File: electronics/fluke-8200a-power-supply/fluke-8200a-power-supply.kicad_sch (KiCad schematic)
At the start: 66 parts, among them J1 Conn_01x08, J2 Conn_01x03, Q1 NPN, Q10 NPN, Q11 2N3055, Q12 NPN, Q13 NPN, Q2 NPN, Q3 NPN, Q4 NPN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

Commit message: only need correct transistors now
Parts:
- removed J2: Conn_01x03, symbol Connector_Generic:Conn_01x03
- removed Q6: NPN, symbol Simulation_SPICE:NPN
- removed R15: R_US, symbol Device:R_US
- added C13: 0.01uF, symbol Device:C
- added J2: Conn_02x03_Counter_Clockwise, symbol Connector_Generic:Conn_02x03_Counter_Clockwise
- added Q6: PNP, symbol Simulation_SPICE:PNP
- C1: value C -> 8uF
- C10, C11, C6, C7, C8, C9: value C -> 1000uF
- C12: value C -> 0.047uF
- C2: value C -> 400
- C3: value C -> 125uF
- C4: value C -> 400uF
- C5: value C -> 125
- R1: value R_US -> 510
- R10: value R_US -> 5.1K
- R11: value R_US -> 78.7K
- R12: value R_Potentiometer_Trim_US -> 10K
- R13: renamed from R21; value R_US -> 59.0K
- R14: value R_US -> 10.0K
- R16, R6: value R_US -> 33
- R18: renamed from R12; value R_US -> 9.09K
- R19: renamed from R13; value R_US -> 33K
- R2: value R_US -> 33K
- R21: renamed from R20; value R_US -> 4.7K
- R22: renamed from R19; value R_US -> 5.6K
- R23: renamed from R18; value R_US -> 10K
- R24: renamed from R17; value R_US -> 33.2K
- R3: value R_US -> 182K
- R4: value R_US -> 15.4K
- R5, R7: value R_US -> 1M
- R8: value R_US -> 470K
- R9: value R_US -> 4.7K
- renumbered D13 to D10, D9 to D13, D10 to D14, D12 to D15, D11 to D16, D14 to D9
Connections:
- net at D15.1 (K): now also D13.2 (A), J1.4 (Pin_4); no longer D16.1 (K)
- net GND: now reaches D15.2 (A)
- net GND: now also C1.1, C10.2, C11.2, C6.2, C7.2, C8.2, C9.2, D1.2 (A), D16.2 (A), D3.2 (A), Q13.3 (E), J2.2 (Pin_2)
- net +5V: now reaches TP5.1
- net +5V: now also Q11.2 (E), R22.2, R23.2, J2.6 (Pin_6)
- net GNDS: now reaches TP3.1
- net GNDS: now also C12.1, C2.1, C3.1, C4.2, C5.1, D9.2 (A), J1.8 (Pin_8), Q7.1 (C), R13.2, R4.1, J2.5 (Pin_5), Q6.3 (E)
- net at C7.1: now also C10.1, C11.1, C6.1, C8.1, C9.1, D13.1 (K), D14.1 (K), Q11.3 (C), Q12.1 (C)
- net +200V: now reaches R5.1
- net +200V: now also Q1.3 (E), R3.2, TP1.1, J2.3 (Pin_3)
- net at R5.2: now also C12.2, R7.1
- net at R23.1: now also Q13.2 (B), R24.2
- net at Q5.1 (C): now also Q4.2 (B), R7.2
- net at Q5.2 (B): now also R12.2
- net at Q5.3 (E): now also D9.1 (K), R10.2
- net at R8.1: now also D10.2 (A), Q7.3 (E), Q6.2 (B)
- net at R8.2: now also Q10.3 (E), R16.2
- net at R1.1: now also C1.2, D2.1 (K), D4.1 (K), R2.1
- net at R1.2: now also Q1.1 (C); no longer R3.2
- net at R12.1: now also R13.1
- net at R12.3: now also R11.2
- net at D6.2 (A): now also D5.1 (K), J1.7 (Pin_7); no longer D5.2 (A)
- net at R22.1: now also Q11.1 (B), Q12.3 (E)
- net at D1.1 (K): now also D2.2 (A), J1.3 (Pin_3); no longer D2.1 (K)
- net at D7.2 (A): now also C4.1, D5.2 (A), R16.1; no longer D8.2 (A)
- net at Q1.2 (B): now also Q2.1 (C), R2.2
- net at R6.1: now also C2.2, D6.1 (K), D8.1 (K)
- net at R6.2: now also Q3.1 (C), Q4.1 (C)
- net at Q3.2 (B): now also Q4.3 (E)
- net +15V: now reaches Q3.3 (E)
- net +15V: now also C3.2, Q2.3 (E), R10.1, R11.1, R14.1, R21.2, TP2.1, J2.1 (Pin_1)
- net at D10.1 (K): now also R19.2
- net at R14.2: now also Q7.2 (B), R18.2, C13.1
- net at Q12.2 (B): now also Q13.1 (C), R21.1
- net -15V: now reaches R18.1
- net -15V: now also C5.2, Q10.1 (C), R19.1, R24.1, TP4.1, C13.2, J2.4 (Pin_4)
- net at J1.6 (Pin_6): now also D7.1 (K), D8.2 (A); no longer D14.1 (K)
- net at Q10.2 (B): now also R9.2
- net at R9.1: now also Q6.1 (C)
- net at Q2.2 (B): now also R3.1, R4.2
- new net: D3.1 (K), D4.2 (A), J1.2 (Pin_2)
- new net: D14.2 (A), D16.1 (K), J1.5 (Pin_5)
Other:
- moved on the sheet: C1, C12, C2, C3, C4, C5, C6, D1, D10, D13, D14, D15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

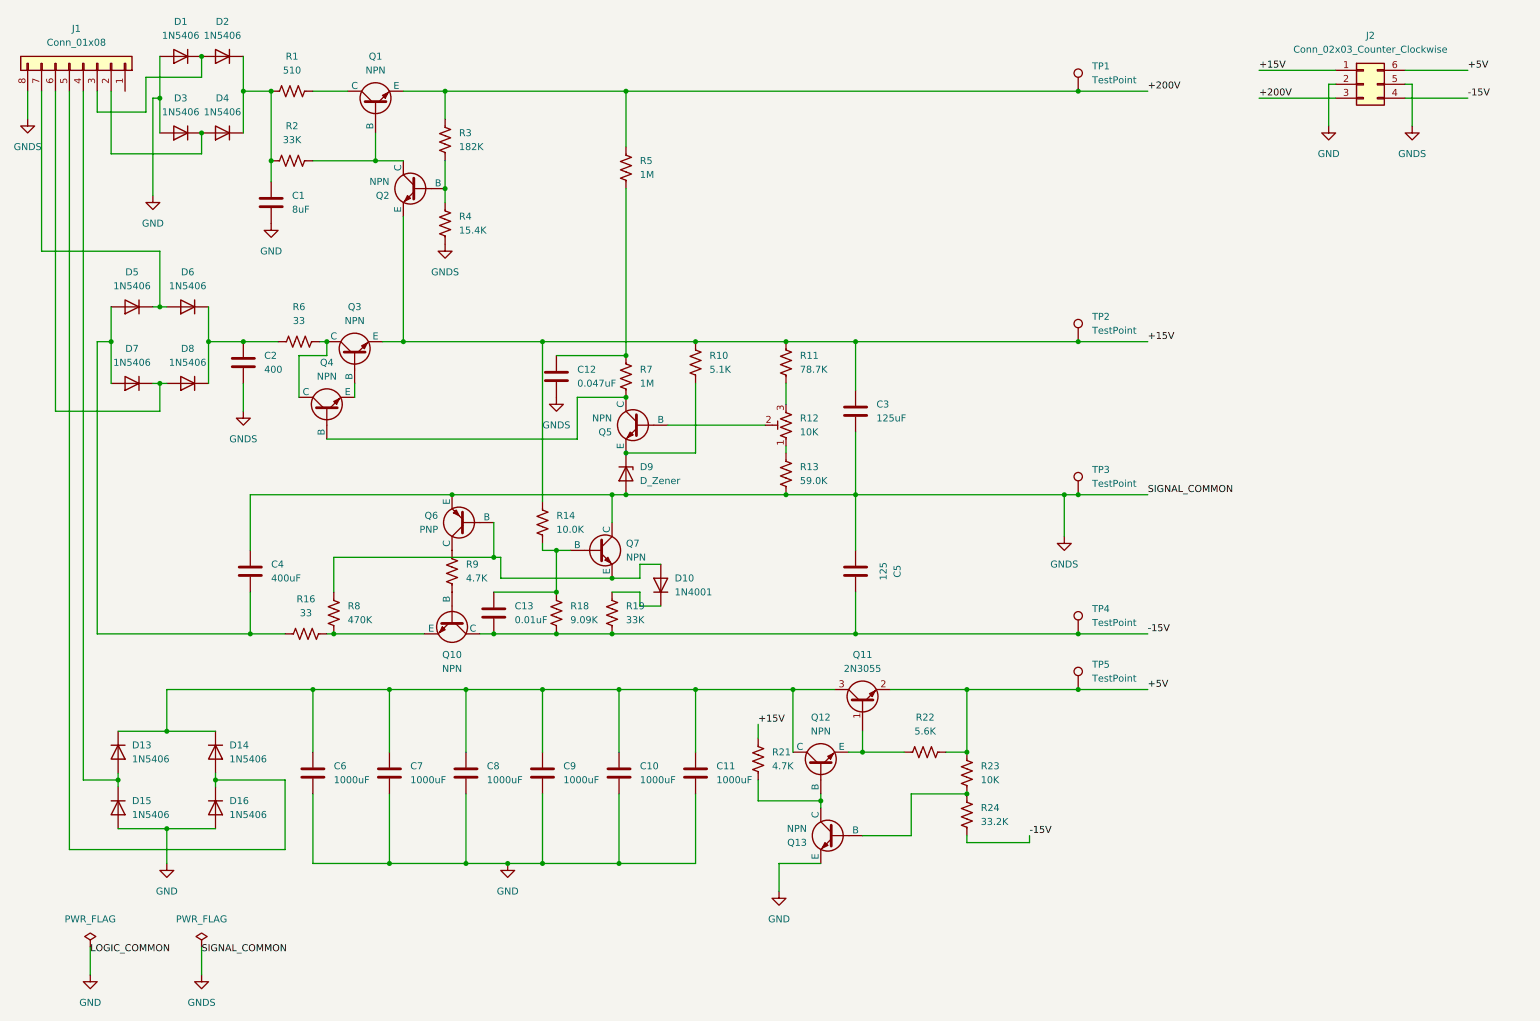
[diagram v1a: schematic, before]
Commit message: changed to pin headers
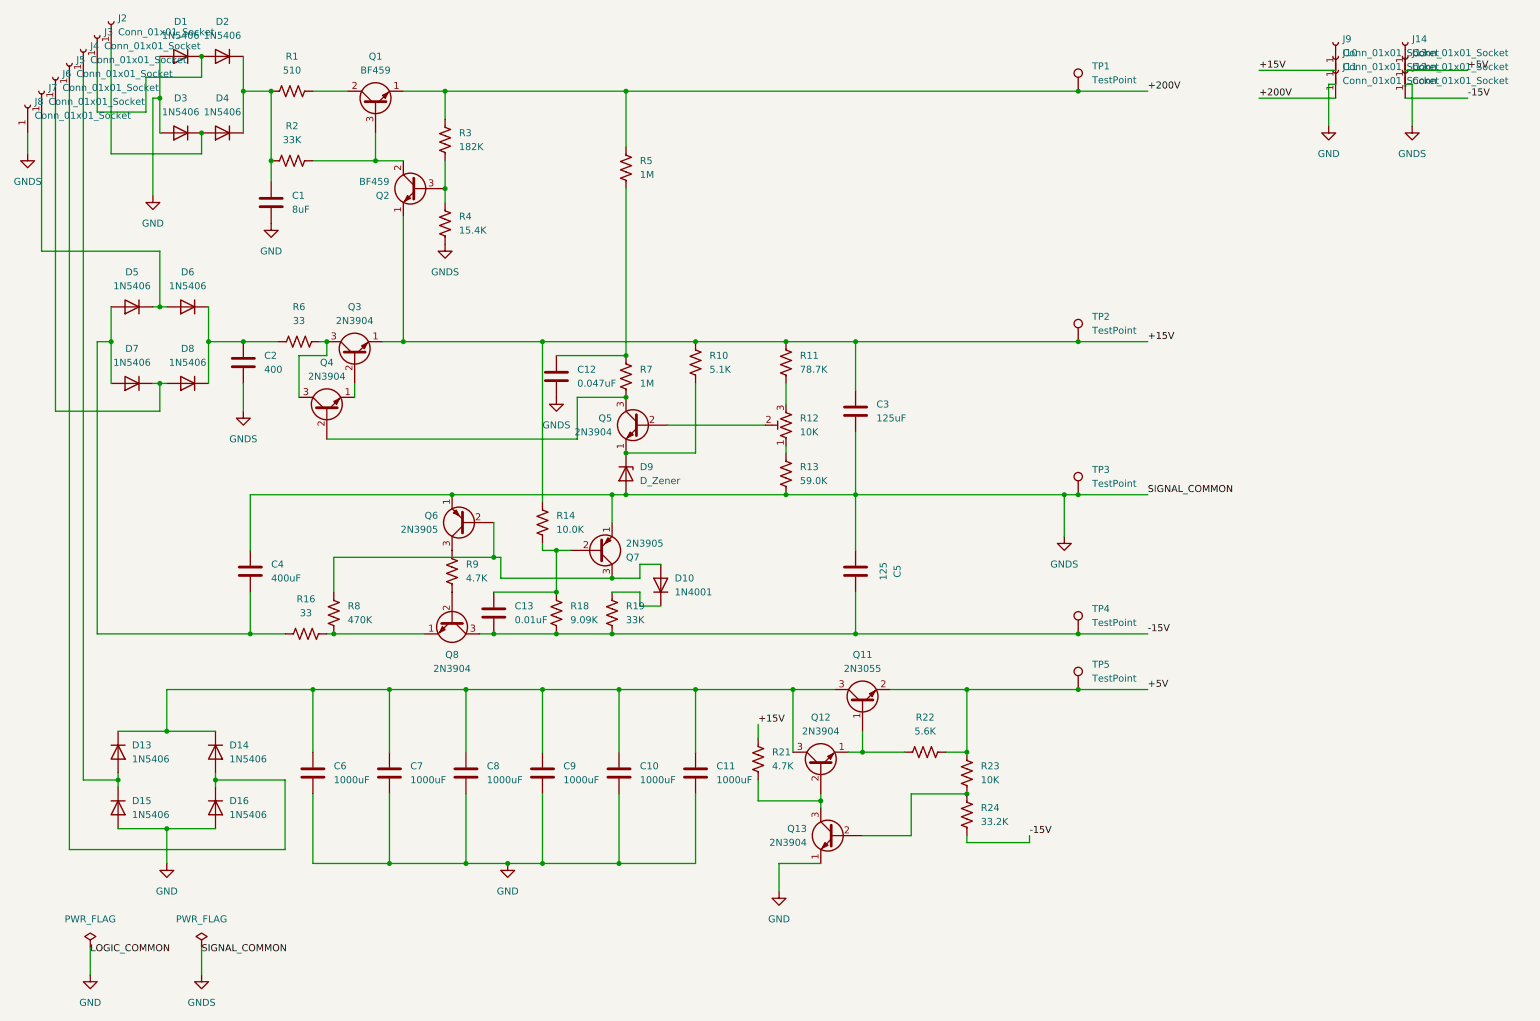
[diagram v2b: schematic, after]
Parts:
- removed J1: Conn_01x08, symbol Connector_Generic:Conn_01x08
- removed J2: Conn_02x03_Counter_Clockwise, symbol Connector_Generic:Conn_02x03_Counter_Clockwise
- removed Q1, Q10, Q12, Q13, Q2, Q3, Q4, Q5, Q7: NPN, symbol Simulation_SPICE:NPN
- removed Q6: PNP, symbol Simulation_SPICE:PNP
- added J10, J11, J12, J13, J14, J2, J3, J4, J5, J6, J7, J8, J9: Conn_01x01_Socket, Connector_PinSocket_2.54mm:PinSocket_1x01_P2.54mm_Vertical, symbol Connector:Conn_01x01_Socket
- added Q1, Q2: BF459, Package_TO_SOT_THT:TO-126-3_Vertical, symbol Transistor_BJT:BF459
- added Q12, Q13, Q3, Q4, Q5, Q8: 2N3904, Package_TO_SOT_THT:TO-92_Inline, symbol Transistor_BJT:2N3904
- added Q6, Q7: 2N3905, Package_TO_SOT_THT:TO-92_Inline, symbol Transistor_BJT:2N3905
- C1: footprint (none) -> Capacitor_THT:CP_Axial_L37.0mm_D13.0mm_P43.00mm_Horizontal
- C10, C11, C2, C4, C6, C7, C8, C9: footprint (none) -> Capacitor_THT:CP_Axial_L30.0mm_D10.0mm_P35.00mm_Horizontal
- C12: footprint (none) -> Capacitor_THT:C_Rect_L13.0mm_W4.0mm_P10.00mm_FKS3_FKP3_MKS4
- C13: footprint (none) -> Capacitor_THT:C_Disc_D8.0mm_W2.5mm_P5.00mm
- C3, C5: footprint (none) -> Capacitor_THT:CP_Axial_L18.0mm_D8.0mm_P25.00mm_Horizontal
- D10: footprint Diode_THT:D_DO-41_SOD81_P10.16mm_Horizontal -> Diode_THT:D_DO-41_SOD81_P12.70mm_Horizontal
- D9: footprint (none) -> Diode_THT:D_A-405_P12.70mm_Horizontal
- R1: footprint (none) -> Resistor_THT:R_Axial_DIN0614_L14.3mm_D5.7mm_P15.24mm_Horizontal
- R10, R11, R13, R14, R16, R18, R19, R2, R21, R22, R23, R24, R3, R4, R5, R6, R7, R8, R9: footprint (none) -> Resistor_THT:R_Axial_DIN0309_L9.0mm_D3.2mm_P12.70mm_Horizontal
- R12: footprint (none) -> Potentiometer_THT:Potentiometer_Runtron_RM-063_Horizontal
- TP1, TP2, TP3, TP4, TP5: footprint (none) -> TestPoint:TestPoint_Loop_D3.50mm_Drill0.9mm_Beaded
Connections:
- net +15V: now also J9.1 (Pin_1), Q2.1 (E), Q3.1 (E)
- net +200V: now also J11.1 (Pin_1), Q1.1 (E)
- net +5V: now also J14.1 (Pin_1)
- net -15V: now also J12.1 (Pin_1), Q8.3 (C)
- net GND: now also J10.1 (Pin_1), Q13.1 (E)
- net GNDS: now also J13.1 (Pin_1), J8.1 (Pin_1), Q6.1 (E), Q7.1 (E)
- net at D13.2 (A), D15.1 (K): now also J4.1 (Pin_1)
- net at C10.1, C11.1, C6.1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: now also Q12.3 (C)
- net at R23.1, R24.2: now also Q13.2 (B)
- net at R7.2: now also Q4.2 (B), Q5.3 (C)
- net at R12.2: now also Q5.2 (B)
- net at D9.1 (K), R10.2: now also Q5.1 (E)
- net at D10.2 (A), R8.1: now also Q6.2 (B), Q7.3 (C)
- net at R16.2, R8.2: now also Q8.1 (E)
- net at R1.2: now also Q1.2 (C)
- net at D3.1 (K), D4.2 (A): now also J2.1 (Pin_1)
- net at D5.1 (K), D6.2 (A): now also J7.1 (Pin_1)
- net at Q11.1 (B), R22.1: now also Q12.1 (E)
- net at D1.1 (K), D2.2 (A): now also J3.1 (Pin_1)
- net at D7.1 (K), D8.2 (A): now also J6.1 (Pin_1)
- net at R2.2: now also Q1.3 (B), Q2.2 (C)
- net at R6.2: now also Q3.3 (C), Q4.3 (C)
- net at C13.1, R14.2, R18.2: now also Q7.2 (B)
- net at R21.1: now also Q12.2 (B), Q13.3 (C)
- net at R9.1: now also Q6.3 (C)
- net at D14.2 (A), D16.1 (K): now also J5.1 (Pin_1)
- net at R9.2: now also Q8.2 (B)
- net at R3.1, R4.2: now also Q2.3 (B)
- new net: Q3.2 (B), Q4.1 (E)
